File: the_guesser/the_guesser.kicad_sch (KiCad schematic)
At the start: 0 parts

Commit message: began work on guesser schematics
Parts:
- added U1: CC1200, Package_DFN_QFN:QFN-32-1EP_5x5mm_P0.5mm_EP3.45x3.45mm, symbol RF:CC1200
- added U2: ESP32-PICO-D4, Package_DFN_QFN:QFN-48-1EP_7x7mm_P0.5mm_EP5.3x5.3mm, symbol MCU_Espressif:ESP32-PICO-D4
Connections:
- new net: U2.1 (VDDA), U2.43 (VDDA), U2.46 (VDDA)
- new net: U2.3 (VDDA3P3), U2.4 (VDDA3P3)

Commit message: created project common symbols library & guesser work
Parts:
- removed U2: ESP32-PICO-D4, Package_DFN_QFN:QFN-48-1EP_7x7mm_P0.5mm_EP5.3x5.3mm, symbol MCU_Espressif:ESP32-PICO-D4
- added C1, C2, C3, C4: C_Small, symbol Device:C_Small
- added J1: USB_B_Mini, symbol Connector:USB_B_Mini
- added X1: SXO53C3A071-40.000M, Crystal:Crystal_SMD_5032-4Pin_5.0x3.2mm, symbol locals:SXO53C3A071-40.000M
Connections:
- net at U1.1 (VDD_GUARD): now also U1.12 (DVDD), U1.5 (DVDD)
- net ~{TXCS}: now reaches U1.11 (~{CS})
- net at U1.21 (DCPL_VCO): now also C2.1
- net at U1.26 (DCPL_PFD_CHP): now also C3.1
- net at U1.29 (DCPL_XOSC): now also C4.1
- net at U1.6 (DCPL): now also C1.1
- net MOSI: now reaches U1.7 (SI)
- net SCLK: now reaches U1.8 (SCLK)
- net MISO: now reaches U1.9 (SO(GPIO1))
- new net GND: J1.4 (ID), J1.5 (GND), J1.6 (Shield)
- new net UD+: J1.3 (D+)
- new net UD-: J1.2 (D-)
- new net V_{USB}: J1.1 (VBUS)
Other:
- note added: "GPIO Strapping Information -------------------------- G00: Boot Mode G03: ROM Messages G45: VDD_SPI Mode G46: JTAG Source"

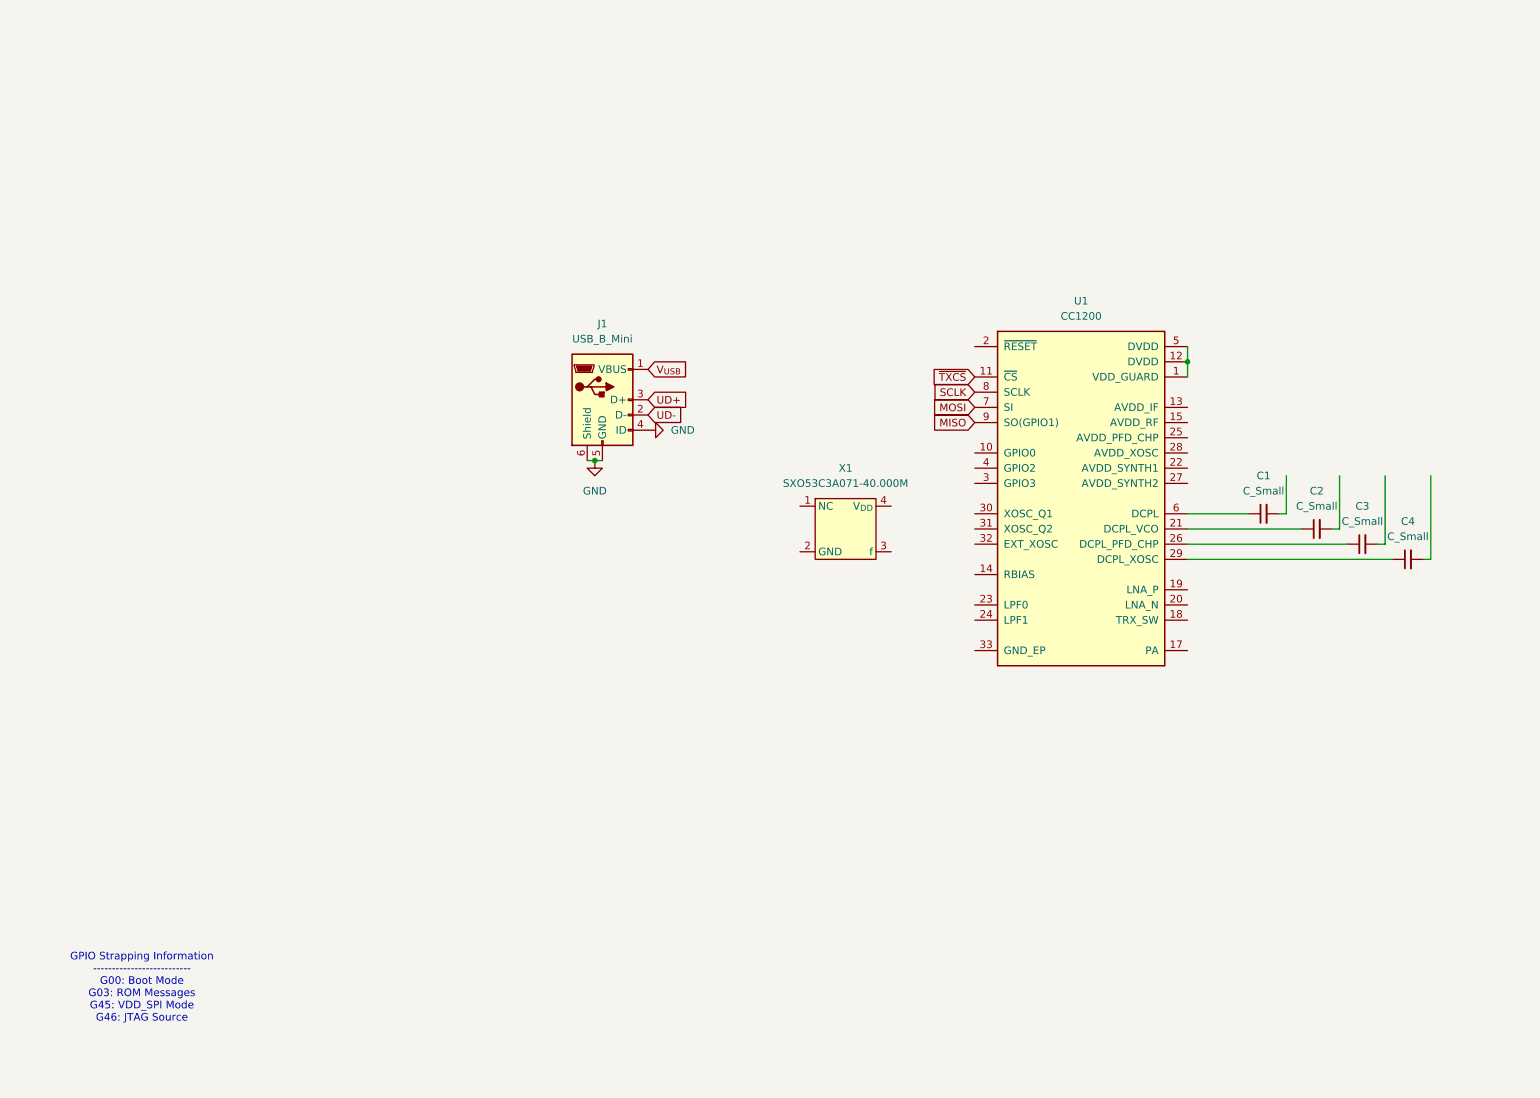
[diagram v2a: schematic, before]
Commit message: placed several chips
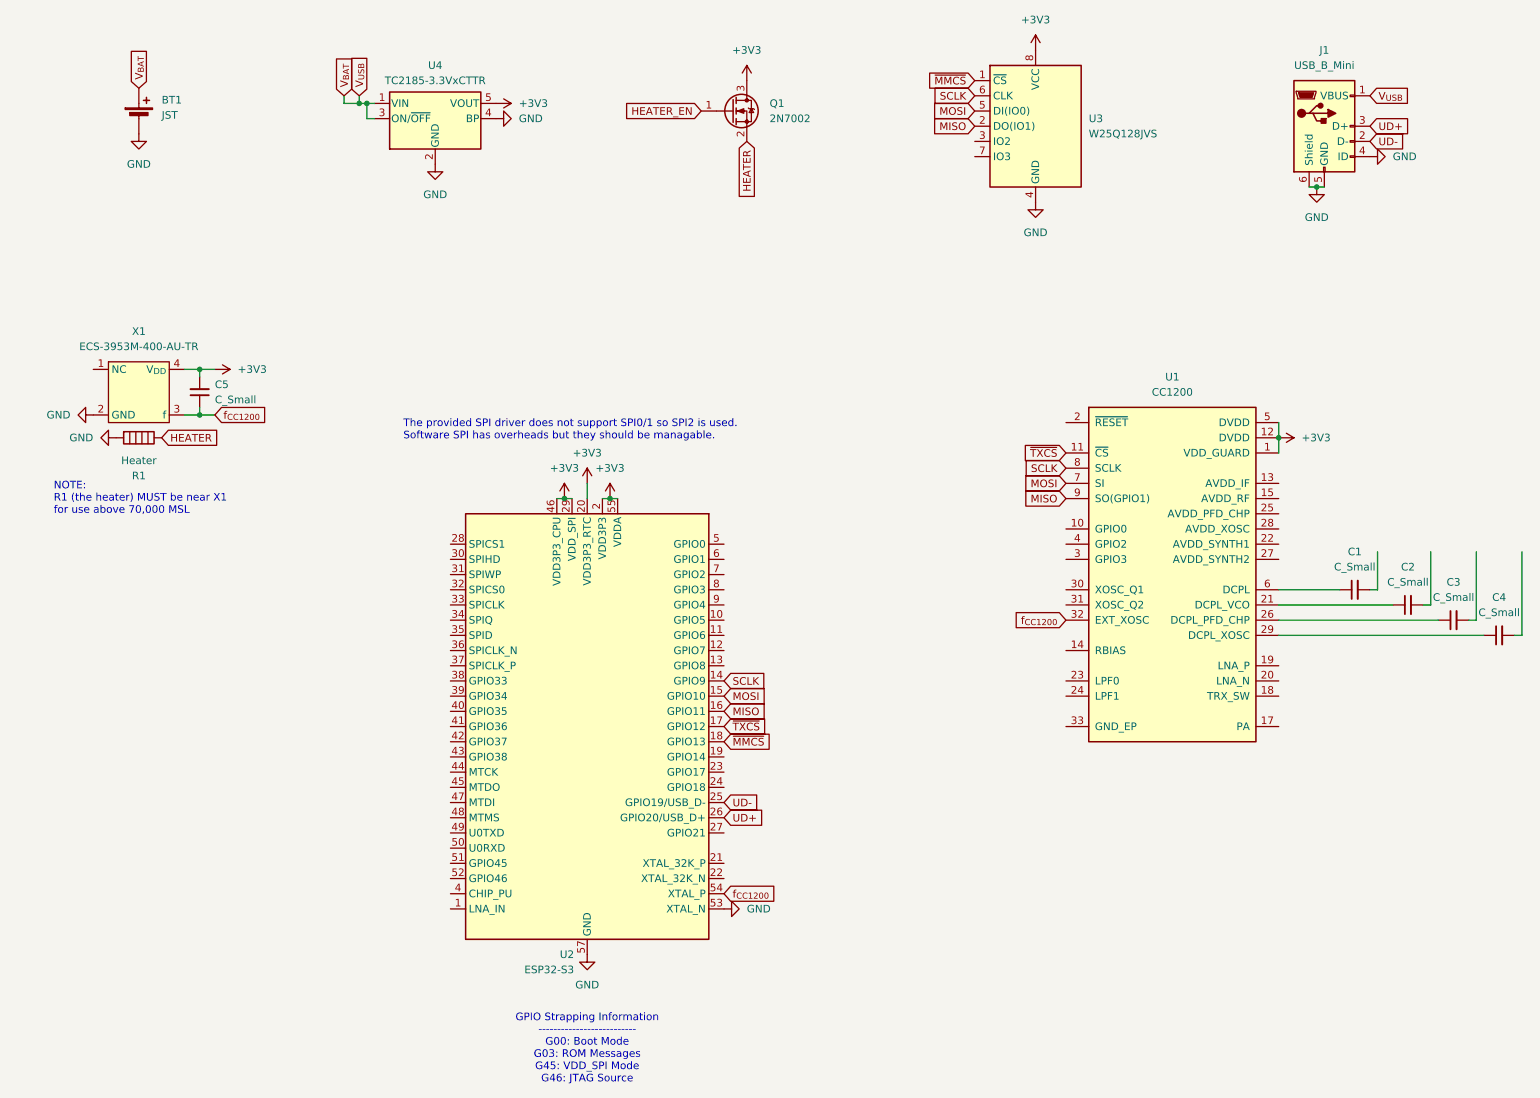
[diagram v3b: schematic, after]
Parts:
- removed X1: SXO53C3A071-40.000M, Crystal:Crystal_SMD_5032-4Pin_5.0x3.2mm, symbol locals:SXO53C3A071-40.000M
- added BT1: JST, locals:TE Right Angle JST, symbol Device:Battery_Cell
- added C5: C_Small, symbol Device:C_Small
- added Q1: 2N7002, Package_TO_SOT_SMD:SOT-23, symbol Transistor_FET:2N7002
- added R1: Heater, symbol Device:Heater
- added U2: ESP32-S3, Package_DFN_QFN:QFN-56-1EP_7x7mm_P0.4mm_EP4x4mm, symbol MCU_Espressif:ESP32-S3
- added U3: W25Q128JVS, Package_SO:SOIC-8_5.23x5.23mm_P1.27mm, symbol Memory_Flash:W25Q128JVS
- added U4: TC2185-3.3VxCTTR, Package_TO_SOT_SMD:SOT-23-5, symbol Regulator_Linear:TC2185-3.3VxCTTR
- added X1: ECS-3953M-400-AU-TR, Crystal:Crystal_SMD_5032-4Pin_5.0x3.2mm, symbol locals:ECS-3953M-400-AU-TR
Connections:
- net GND: now also BT1.2 (-), R1.2, U2.53 (XTAL_N), U2.57 (GND), U3.4 (GND), U4.2 (GND), U4.4 (BP), X1.2 (GND)
- net MISO: now also U2.16 (GPIO11), U3.2 (DO(IO1))
- net MOSI: now also U2.15 (GPIO10), U3.5 (DI(IO0))
- net SCLK: now also U2.14 (GPIO9), U3.6 (CLK)
- net UD+: now also U2.26 (GPIO20/USB_D+)
- net UD-: now also U2.25 (GPIO19/USB_D-)
- net ~{TXCS}: now also U2.17 (GPIO12)
- net +3V3: now reaches U1.1 (VDD_GUARD), U1.12 (DVDD), U1.5 (DVDD)
- net +3V3: now also C5.2, Q1.3 (D), U2.2 (VDD3P3), U2.20 (VDD3P3_RTC), U2.29 (VDD_SPI), U2.3 (VDD3P3), U2.46 (VDD3P3_CPU), U2.55 (VDDA), U2.56 (VDDA), U3.8 (VCC), U4.5 (VOUT), X1.4 (V_{DD})
- net f_{CC1200}: now reaches U1.32 (EXT_XOSC)
- net f_{CC1200}: now also C5.1, U2.54 (XTAL_P), X1.3 (f)
- net V_{USB} renamed V_{BAT}
- net V_{BAT}: now also BT1.1 (+), U4.1 (VIN), U4.3 (ON/~{OFF})
- new net HEATER: Q1.2 (S), R1.1
- new net HEATER_EN: Q1.1 (G)
- new net ~{MMCS}: U2.18 (GPIO13), U3.1 (~{CS})
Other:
- note added: "NOTE: R1 (the heater) MUST be near X1 for use above 70,000 MSL"
- note added: "The provided SPI driver does not support SPI0/1 so SPI2 is used. Software SPI has overheads but they should be managable."
- company: (none) -> Mines Rocket Club
- title: (none) -> The Guesser
- moved on the sheet: C1, C2, C3, C4, J1, U1

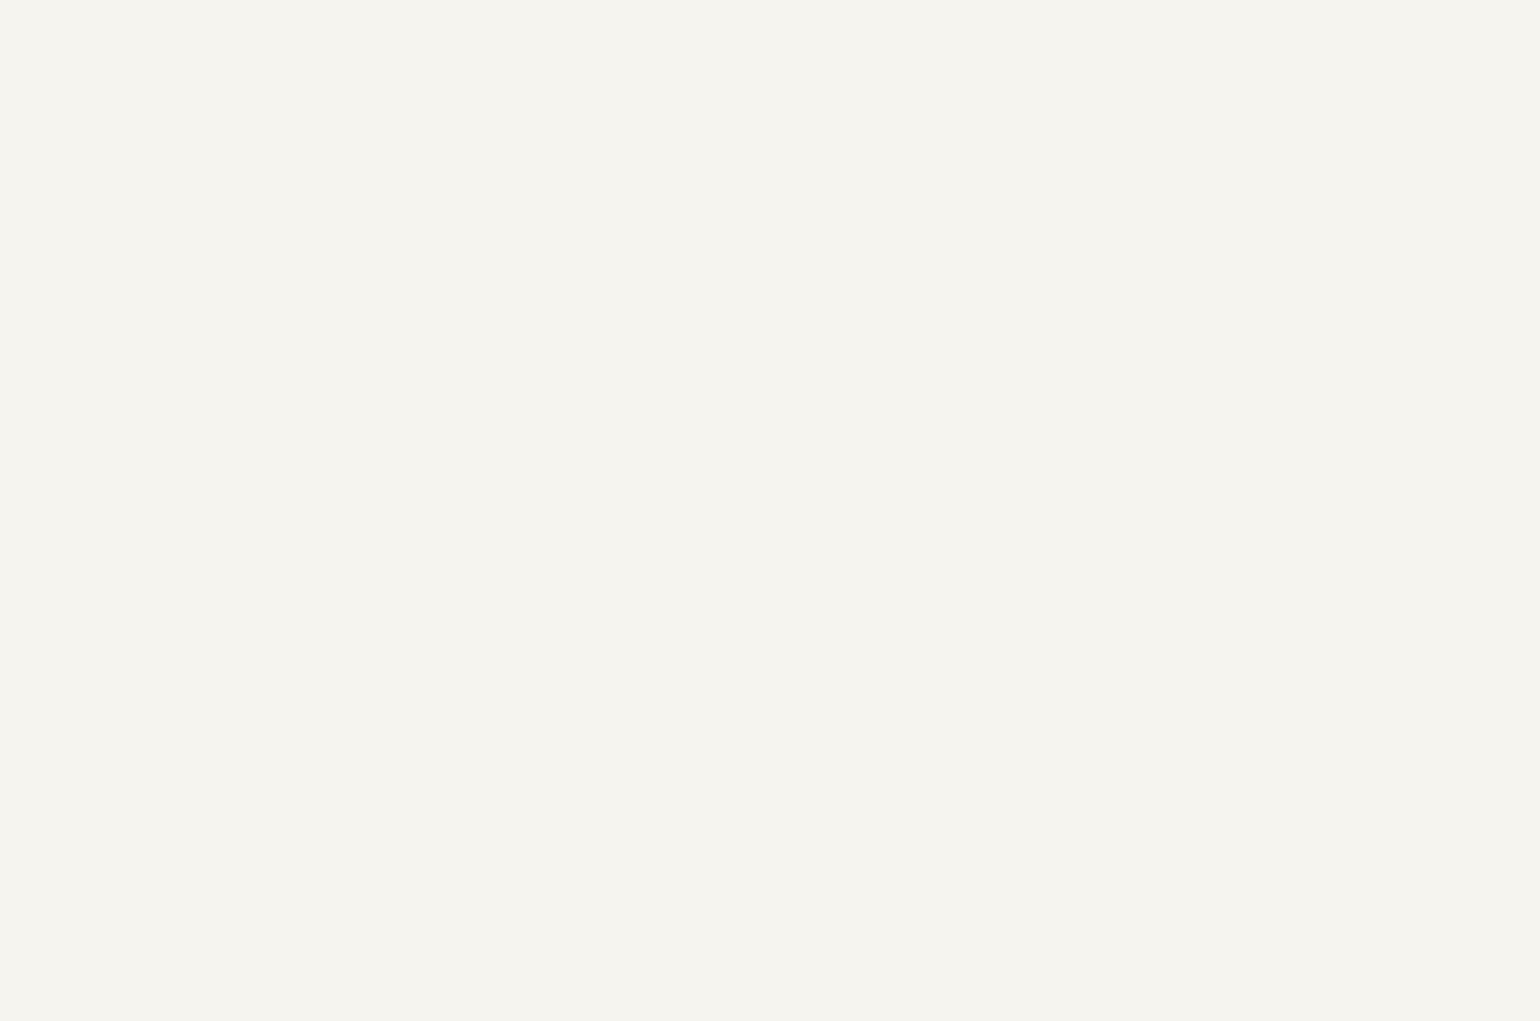
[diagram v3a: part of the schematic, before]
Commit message: Fixed custom symbol file paths
In addition to fixing all the file paths I also updated some symbols on the Timer and Screamer, updated the board characteristic tables, added missing 3D models to some components, and did a bit of other file stuff.
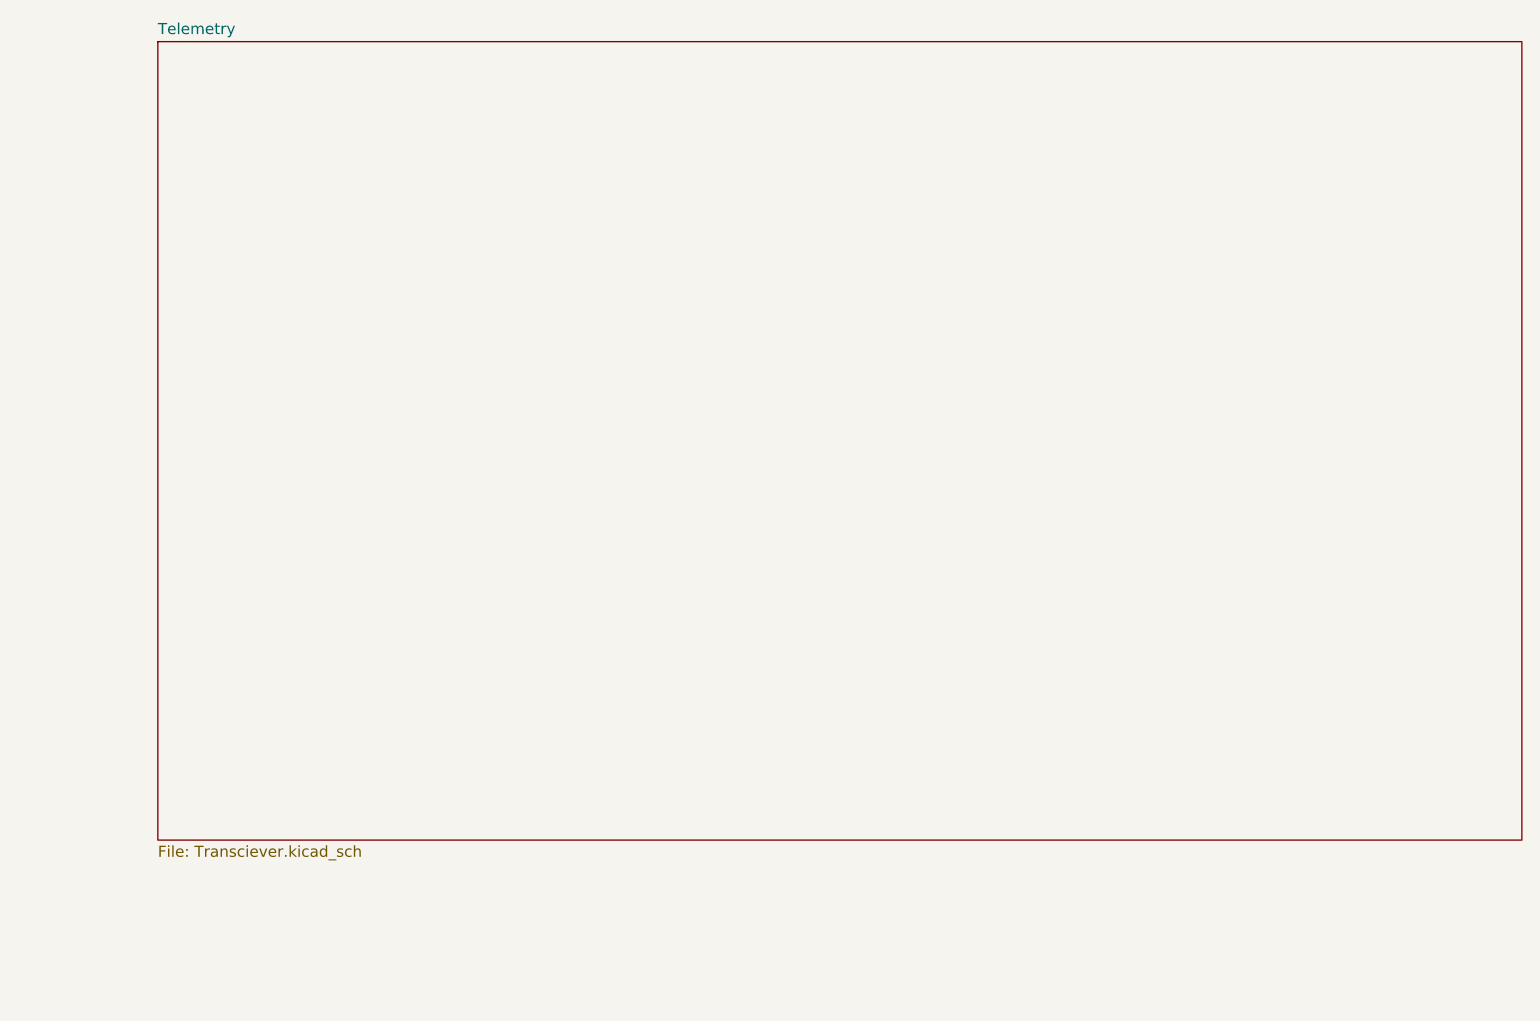
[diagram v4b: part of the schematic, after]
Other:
- added sheet Telemetry (Transciever.kicad_sch)
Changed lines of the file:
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@@
 	(title_block
 		(title "The Guesser")
-		(date "2024-04-10")
+		(date "2024-05-16")
 		(rev "0.0.1")
 		(company "Mines Rocket Club")
@@
 				)
 			)
+		)
+	)
+	(sheet
+		(at 306.07 13.97)
+		(size 156.21 91.44)
+		(fields_autoplaced yes)
+		(stroke
+			(width 0.1524)
+			(type solid)
+		)
+		(fill
+			(color 0 0 0 0.0000)
+		)
+		(property "Sheetname" "Telemetry"
+			(at 306.07 13.2584 0)
+			(effects
+				(font
+					(size 1.27 1.27)
+				)
+				(justify left bottom)
+			)
+		)
+		(property "Sheetfile" "Transciever.kicad_sch"
+			(at 306.07 105.9946 0)
+			(effects
+				(font
+					(size 1.27 1.27)
+				)
+				(justify left top)
+			)
+		)
+		(instances
+			(project "the_guesser"
+				(path "/473e3a2e-6c5e-4995-af4a-e4bf1449cab0"
+					(page "2")
+				)
+			)

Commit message: Started on Guesser transmitter schematic
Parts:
- removed C1, C2, C3, C4: C_Small, symbol Device:C_Small
- added H1, H2, H3, H4: MountingHole, MountingHole:MountingHole_3.2mm_M3, symbol Mechanical:MountingHole
- J1: footprint (none) -> Connector_USB:USB_Mini-B_Wuerth_65100516121_Horizontal
- Q1, U1, U4: now not fitted; now left out of the parts list
- renumbered X1 to X2
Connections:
- net ~{TXCS}: no longer U2.17 (GPIO12)
- net UD+ renamed USB_D+
- net UD- renamed USB_D-
- new net ~{CS}: U2.17 (GPIO12)
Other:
- sheet Telemetry renamed Transmitter
- sheet Transmitter: file Transciever.kicad_sch -> Guesser_Transciever.kicad_sch
- title: The Guesser -> Guesser

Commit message: Started Guesser sensor selection
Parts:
- removed BT1: JST, locals:TE Right Angle JST, symbol Device:Battery_Cell
- removed U1: CC1200, Package_DFN_QFN:QFN-32-1EP_5x5mm_P0.5mm_EP3.45x3.45mm, symbol RF:CC1200
- removed U4: TC2185-3.3VxCTTR, Package_TO_SOT_SMD:SOT-23-5, symbol Regulator_Linear:TC2185-3.3VxCTTR
- added BT1: Battery_Cell, locals_but_working_PLEASE:CONN2_1775469-2_TEC, symbol Custom_Flight_Computer_Symbols:1775469-2
- added C4: 10u, Capacitor_SMD:C_0603_1608Metric, symbol Device:C
- added D1: MB6S, Package_TO_SOT_SMD:TO-269AA, symbol Diode_Bridge:MB6S
- added J4, J5: Screw_Terminal_01x06, TerminalBlock_Phoenix:TerminalBlock_Phoenix_MPT-0,5-6-2.54_1x06_P2.54mm_Horizontal, symbol Connector:Screw_Terminal_01x06
- added L3: 0.47u, Inductor_SMD:L_0603_1608Metric, symbol Device:L_Small
- added R2: 5.36k, Resistor_SMD:R_0603_1608Metric, symbol Device:R_Small_US
- added R3: 1.2k, Resistor_SMD:R_0603_1608Metric, symbol Device:R_Small_US
- added U10: TPS61033DRLR, Package_TO_SOT_SMD:SOT-583-8, symbol globals:TPS61033
- C5, R1, X2: now not fitted; now left out of the parts list
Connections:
- net GND: now also C4.2, D1.4 (-), R3.2, U10.6 (GND)
- net V_{BAT} renamed V_{USB}
- new net: R2.2, R3.1, U10.5 (FB)
- new net: L3.1, U10.7 (SW)
- new net BT+: BT1.2, D1.2
- new net BT-: BT1.1, D1.1
- new net VCC: C4.1, R2.1, U10.4 (PG), U10.8 (VOUT)
- new net V_{B}: D1.3 (+), L3.2, U10.1 (VIN), U10.2 (EN), U10.3 (MODE)
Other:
- added sheet Sensors (Guesser_Sensors.kicad_sch)

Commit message: Started Guesser I/O and continued sensor selection
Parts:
- removed J1: USB_B_Mini, Connector_USB:USB_Mini-B_Wuerth_65100516121_Horizontal, symbol Connector:USB_B_Mini
- removed J4, J5: Screw_Terminal_01x06, TerminalBlock_Phoenix:TerminalBlock_Phoenix_MPT-0,5-6-2.54_1x06_P2.54mm_Horizontal, symbol Connector:Screw_Terminal_01x06
- renumbered U2 to U1, U3 to U11
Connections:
- net +3V3: no longer U1.2 (VDD3P3), U1.20 (VDD3P3_RTC), U1.29 (VDD_SPI), U1.3 (VDD3P3), U1.46 (VDD3P3_CPU), U1.55 (VDDA), U1.56 (VDDA), U11.8 (VCC)
- net GND: no longer U1.53 (XTAL_N)
- net VCC: now also U11.8 (VCC)
- net f_{CC1200}: no longer U1.54 (XTAL_P)
- net MISO renamed SDO2
- net MOSI renamed SDI2
- net SCLK renamed SCLK2
- net ~{CS}: no longer names the net of U1.17 (GPIO12)
- net ~{MMCS}: no longer names the net of U1.18 (GPIO13)
- net ~{MMCS}: no longer U11.1 (~{CS})
- new net: U1.2 (VDD3P3), U1.3 (VDD3P3)
- new net: U1.55 (VDDA), U1.56 (VDDA)
- new net ~{CS}_{FLASH}: U11.1 (~{CS})
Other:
- added sheet Inputs Outputs (Guesser_IO.kicad_sch)
- note added: "Power Supply"
- moved on the sheet: BT1, C4, C5, D1, H1, H2, H3, H4, L3, Q1, R1, R2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
